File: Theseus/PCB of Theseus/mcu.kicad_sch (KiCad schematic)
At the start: 19 parts, among them J5 Programmer, U6 STM32H750VBTx, U8 MX25L25645G

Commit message: Theseus_Dev_Rev2
It's still the same PCB
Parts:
- removed C10, C11, C12, C13, C14, C15, C22, C9: 100n, Capacitor_SMD:C_0603_1608Metric_Pad1.08x0.95mm_HandSolder, symbol Device:C_Small_US
- removed C16: 4.7u, Capacitor_SMD:C_0603_1608Metric_Pad1.08x0.95mm_HandSolder, symbol Device:C_Small_US
- removed C17: 1u, Capacitor_SMD:C_0402_1005Metric_Pad0.74x0.62mm_HandSolder, symbol Device:C_Small_US
- removed C7, C8: 2.2u, Capacitor_SMD:C_0603_1608Metric_Pad1.08x0.95mm_HandSolder, symbol Device:C_Small_US
- added C10, C11, C12, C13, C14, C15, C22, C9: 100n, Capacitor_SMD:C_0805_2012Metric_Pad1.18x1.45mm_HandSolder, symbol Device:C
- added C16: 4.7u, Capacitor_SMD:C_0805_2012Metric_Pad1.18x1.45mm_HandSolder, symbol Device:C
- added C17: 1n, Capacitor_SMD:C_0805_2012Metric_Pad1.18x1.45mm_HandSolder, symbol Device:C
- added C7, C8: 2.2u, Capacitor_SMD:C_0805_2012Metric_Pad1.18x1.45mm_HandSolder, symbol Device:C
- added FB1: FerriteBead, Resistor_SMD:R_0805_2012Metric_Pad1.20x1.40mm_HandSolder, symbol Device:FerriteBead
- J5: value Programmer -> Programmer GRPB022VWQS-RC
- R44, R45: footprint Resistor_SMD:R_0603_1608Metric_Pad0.98x0.95mm_HandSolder -> Resistor_SMD:R_0805_2012Metric_Pad1.20x1.40mm_HandSolder; symbol Device:R_Small_US -> Device:R_US
- U8: footprint Package_SO:SOIC-16W_7.5x10.3mm_P1.27mm -> Package_SO:SOIC-8_5.3x5.3mm_P1.27mm
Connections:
- net +3.3V: now also U8.8 (VCC), C10.1, C11.1, C12.1, C13.1, C14.1, C15.1, C16.1, C17.1, C9.1, FB1.1; no longer U6.21 (VDDA), U8.2 (VCC)
- net GND: now also U8.4 (GND), C10.2, C11.2, C12.2, C13.2, C14.2, C15.2, C16.2, C17.2, C22.2, C7.2, C8.2, C9.2; no longer U8.10 (GND)
- net LED_BLUE: now also U6.57 (PD10); no longer U6.28 (PA4)
- net LED_RED: now also U6.56 (PD9); no longer U6.29 (PA5)
- net MEM_~{RESET}: now also U8.7 (RESET#/SIO3); no longer U8.3 (RESET#)
- net SPI_MISO: now also U8.2 (SO/SIO1); no longer U8.8 (SO/SIO1)
- net SPI_MOSI: now also U8.5 (SI/SIO0); no longer U8.15 (SI/SIO0)
- net SPI_NSS: now also U8.1 (CS#); no longer U8.7 (CS#)
- net SPI_SCK: now also U8.6 (SCLK); no longer U8.16 (SCLK)
- net at U6.14 (NRST): now also C22.1
- net TC1_SI: now reaches U6.33 (PC5)
- net at U6.48 (VCAP): now also C7.1
- net at U6.73 (VCAP): now also C8.1
- net RTD_1 renamed TC3
- net RTD_2 renamed TC2-
- net RTD_3 renamed TC2+
- new net: FB1.2, U6.21 (VDDA)
- new net TC1_NSS: U6.28 (PA4)
- new net TC1_SCK: U6.29 (PA5)
- no-connect marks 63 -> 52
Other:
- note added: "TC1 using SPI1"
- note added: "Using SPI2 for flash memory"
- note removed: "Using SPI2"

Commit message: Minor routing changes
Still the same PCB
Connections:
- net TC1_SI: now also U6.30 (PA6); no longer U6.33 (PC5)
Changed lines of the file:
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@@
-	)
-	(no_connect
-		(at 115.57 53.34)
 	)
 	(no_connect
 		(at 115.57 66.04)
+	)
+	(no_connect
+		(at 115.57 137.16)
 	)
 	(no_connect
@@
 	(hierarchical_label "TC1_SI"
 		(shape input)
-		(at 115.57 137.16 0)
-		(effects
-			(font
+		(at 115.57 53.34 0)
+		(effects
+			(font

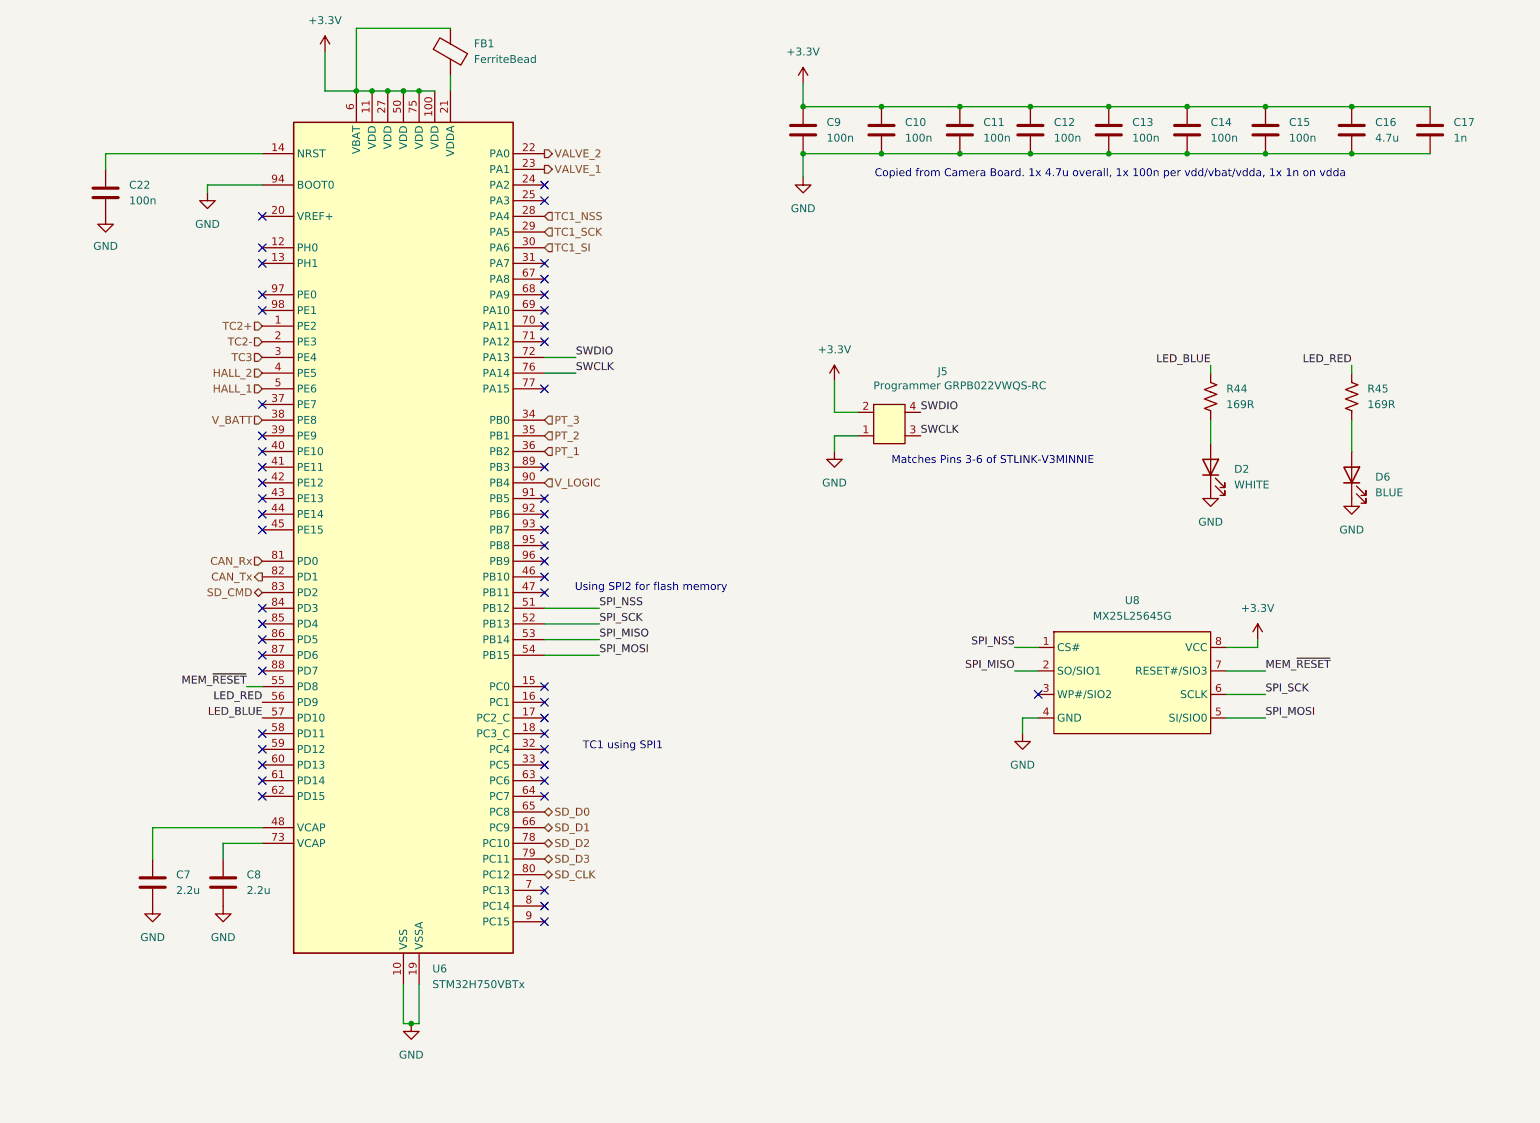
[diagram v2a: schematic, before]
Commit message: Fixes V3
- Copied Ferrite Bead P/N from processor
- Added external oscillator
- Made status LED pins pull-down
- Copied processor programming header
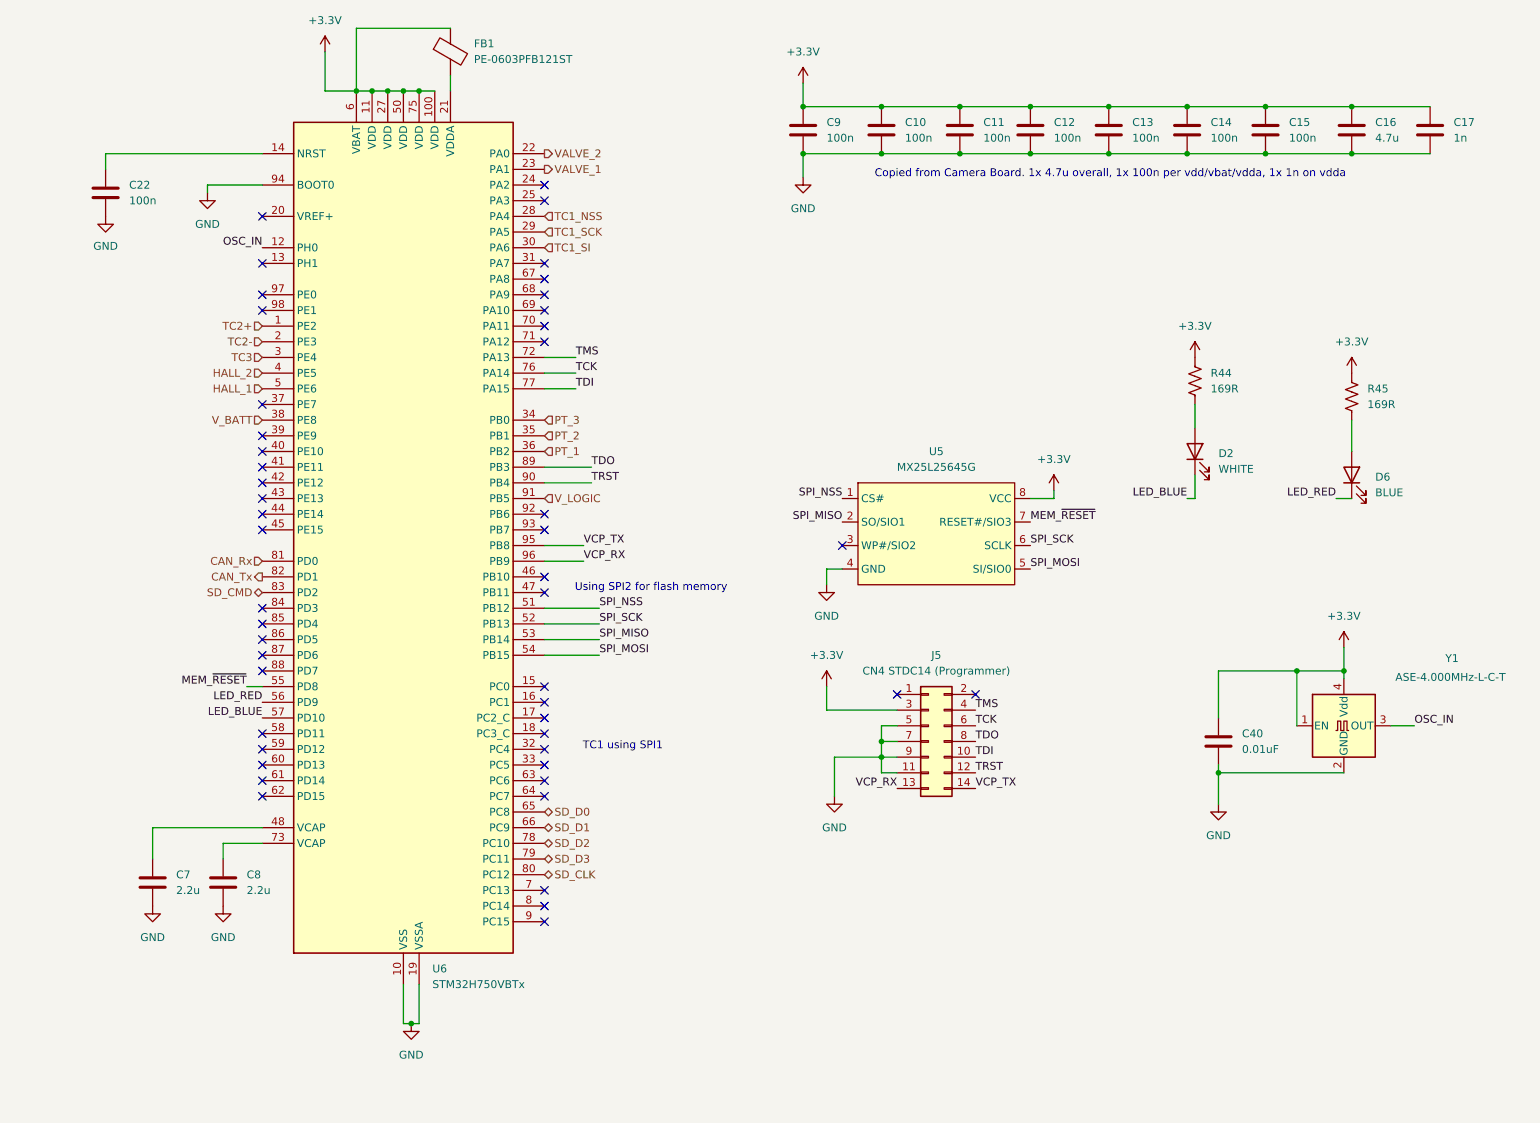
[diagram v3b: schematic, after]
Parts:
- removed J5: Programmer GRPB022VWQS-RC, Connector_PinHeader_1.27mm:PinHeader_2x02_P1.27mm_Vertical_SMD, symbol FYDP_Library:Programmer
- removed U8: MX25L25645G, Package_SO:SOIC-8_5.3x5.3mm_P1.27mm, symbol FYDP_Library:MX25L25645G
- added C40: 0.01uF, Capacitor_SMD:C_0805_2012Metric_Pad1.18x1.45mm_HandSolder, symbol Device:C
- added J5: CN4 STDC14 (Programmer), Connector_PinHeader_1.27mm:PinHeader_2x07_P1.27mm_Vertical_SMD, symbol Connector_Generic:Conn_02x07_Odd_Even
- added U5: MX25L25645G, Package_SO:SOIC-8_5.3x5.3mm_P1.27mm, symbol FYDP_Library:MX25L25645G
- added Y1: ASE-4.000MHz-L-C-T, Oscillator:Oscillator_SMD_Abracon_ASE-4Pin_3.2x2.5mm, symbol Oscillator:ASE-xxxMHz
- D6: footprint Diode_SMD:D_0603_1608Metric_Pad1.05x0.95mm_HandSolder -> Diode_SMD:D_1206_3216Metric_Pad1.42x1.75mm_HandSolder
- FB1: value FerriteBead -> PE-0603PFB121ST; footprint Resistor_SMD:R_0805_2012Metric_Pad1.20x1.40mm_HandSolder -> Resistor_SMD:R_0603_1608Metric_Pad0.98x0.95mm_HandSolder
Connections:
- net +3.3V: now also R44.1, R45.1, C40.1, J5.3 (Pin_3), U5.8 (VCC), Y1.1 (EN), Y1.4 (Vdd)
- net GND: now also C40.2, J5.11 (Pin_11), J5.5 (Pin_5), J5.7 (Pin_7), J5.9 (Pin_9), U5.4 (GND), Y1.2 (GND); no longer D2.1 (K), D6.1 (K)
- net LED_BLUE: now also D2.1 (K); no longer R44.1
- net LED_RED: now also D6.1 (K); no longer R45.1
- net MEM_~{RESET}: now also U5.7 (RESET#/SIO3)
- net SPI_MISO: now also U5.2 (SO/SIO1)
- net SPI_MOSI: now also U5.5 (SI/SIO0)
- net SPI_NSS: now also U5.1 (CS#)
- net SPI_SCK: now also U5.6 (SCLK)
- net V_LOGIC: now also U6.91 (PB5); no longer U6.90 (PB4)
- net OSC_IN: now reaches U6.12 (PH0)
- net OSC_IN: now also Y1.3 (OUT)
- net TDI: now reaches U6.77 (PA15)
- net TDI: now also J5.10 (Pin_10)
- net TDO: now reaches U6.89 (PB3)
- net TDO: now also J5.8 (Pin_8)
- net VCP_TX: now reaches U6.95 (PB8)
- net VCP_TX: now also J5.14 (Pin_14)
- net VCP_RX: now reaches U6.96 (PB9)
- net VCP_RX: now also J5.13 (Pin_13)
- net SWCLK renamed TCK
- net TCK: now also J5.6 (Pin_6)
- net SWDIO renamed TMS
- net TMS: now also J5.4 (Pin_4)
- new net TRST: J5.12 (Pin_12), U6.90 (PB4)
- no-connect marks 52 -> 48
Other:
- note removed: "Matches Pins 3-6 of STLINK-V3MINNIE"
- moved on the sheet: D2, R44

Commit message: Flight design, first pass
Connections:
- net PT_1: now also U6.35 (PB1); no longer U6.36 (PB2)
- net PT_2: now also U6.36 (PB2); no longer U6.35 (PB1)
- net TC2+: no longer names the net of U6.1 (PE2)
- net TC2-: no longer names the net of U6.2 (PE3)
- net TC3: no longer names the net of U6.3 (PE4)
- no-connect marks 48 -> 51
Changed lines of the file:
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@@
 	(text "TC1 using SPI1"
 		(exclude_from_sim no)
-		(at 128.27 134.112 0)
+		(at 125.476 56.388 0)
 		(effects
 			(font
@@
 	)
 	(no_connect
+		(at 69.85 68.58)
+	)
+	(no_connect
+		(at 69.85 66.04)
+	)
+	(no_connect
 		(at 69.85 96.52)
 	)
@@
 	(no_connect
 		(at 69.85 48.26)
+	)
+	(no_connect
+		(at 69.85 71.12)
 	)
 	(no_connect
@@
 		)
 	)
-	(hierarchical_label "TC3"
-		(shape input)
-		(at 69.85 71.12 180)
-		(effects
-			(font
-				(size 1.27 1.27)
-			)
-			(justify right)
-		)
-	)
 	(hierarchical_label "TC1_NSS"
 		(shape input)
@@
 		)
 	)
-	(hierarchical_label "TC2+"
-		(shape input)
-		(at 69.85 66.04 180)
-		(effects
-			(font
-				(size 1.27 1.27)
-			)
-			(justify right)
-		)
-	)
 	(hierarchical_label "PT_1"
 		(shape input)
-		(at 115.57 86.36 0)
+		(at 115.57 83.82 0)
 		(effects
 			(font
@@
 	(hierarchical_label "PT_2"
 		(shape input)
-		(at 115.57 83.82 0)
+		(at 115.57 86.36 0)
 		(effects
 			(font
@@
 		)
 	)
-	(hierarchical_label "TC2-"
-		(shape input)
-		(at 69.85 68.58 180)
-		(effects
-			(font
-				(size 1.27 1.27)
-			)
-			(justify right)
-		)
-	)

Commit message: Flight design v1
First pass at flight design
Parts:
- C10, C11, C12, C13, C14, C15, C16, C17, C22, C40, C7, C8, C9: footprint Capacitor_SMD:C_0805_2012Metric_Pad1.18x1.45mm_HandSolder -> Capacitor_SMD:C_0603_1608Metric_Pad1.08x0.95mm_HandSolder
- D2, D6: footprint Diode_SMD:D_1206_3216Metric_Pad1.42x1.75mm_HandSolder -> Diode_SMD:D_0603_1608Metric_Pad1.05x0.95mm_HandSolder
- J5: footprint Connector_PinHeader_1.27mm:PinHeader_2x07_P1.27mm_Vertical_SMD -> Connector_PinSocket_1.27mm:PinSocket_2x07_P1.27mm_Vertical_SMD
- R44, R45: footprint Resistor_SMD:R_0805_2012Metric_Pad1.20x1.40mm_HandSolder -> Resistor_SMD:R_0603_1608Metric_Pad0.98x0.95mm_HandSolder
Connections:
- net PT_1: now also U6.36 (PB2); no longer U6.35 (PB1)
- net PT_2: now also U6.35 (PB1); no longer U6.36 (PB2)
- net PT6: now reaches U6.40 (PE10)
- net PT5: now reaches U6.41 (PE11)
- net PT4: now reaches U6.42 (PE12)
- no-connect marks 51 -> 48
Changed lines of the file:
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@@
 	(text "TC1 using SPI1"
 		(exclude_from_sim no)
-		(at 125.476 56.388 0)
+		(at 134.112 51.308 0)
 		(effects
 			(font
@@
 	)
 	(no_connect
-		(at 69.85 86.36)
+		(at 69.85 116.84)
 	)
 	(no_connect
@@
 	)
 	(no_connect
-		(at 69.85 121.92)
-	)
-	(no_connect
-		(at 69.85 116.84)
+		(at 172.72 125.73)
 	)
 	(no_connect
-		(at 172.72 125.73)
+		(at 69.85 119.38)
 	)
 	(no_connect
@@
 	)
 	(no_connect
-		(at 69.85 88.9)
-	)
-	(no_connect
 		(at 115.57 129.54)
 	)
@@
 	)
 	(no_connect
-		(at 69.85 91.44)
-	)
-	(no_connect
 		(at 69.85 134.62)
 	)
@@
 	)
 	(no_connect
-		(at 69.85 119.38)
-	)
-	(no_connect
 		(at 69.85 55.88)
 	)
@@
 	)
 	(no_connect
+		(at 69.85 121.92)
+	)
+	(no_connect
 		(at 115.57 137.16)
 	)
@@
 		)
 	)
+	(hierarchical_label "PT6"
+		(shape input)
+		(at 69.85 86.36 180)
+		(effects
+			(font
+				(size 1.27 1.27)
+			)
+			(justify right)
+		)
+	)
 	(hierarchical_label "V_BATT"
 		(shape input)
@@
 	(hierarchical_label "PT_1"
 		(shape input)
-		(at 115.57 83.82 0)
+		(at 115.57 86.36 0)
 		(effects
 			(font
@@
 	(hierarchical_label "PT_2"
 		(shape input)
-		(at 115.57 86.36 0)
+		(at 115.57 83.82 0)
 		(effects
 			(font
@@
 		)
 	)
+	(hierarchical_label "PT4"
+		(shape input)
+		(at 69.85 91.44 180)
+		(effects
+			(font
+				(size 1.27 1.27)
+			)
+			(justify right)
+		)
+	)
 	(hierarchical_label "TC1_SI"
 		(shape input)
@@
 		)
 	)
+	(hierarchical_label "PT5"
+		(shape input)
+		(at 69.85 88.9 180)
+		(effects
+			(font
+				(size 1.27 1.27)
+			)
+			(justify right)
+		)
+	)
 	(symbol
 		(lib_id "Device:C")
@@
 			)
 		)
-		(property "Footprint" "Capacitor_SMD:C_0805_2012Metric_Pad1.18x1.45mm_HandSolder"
+		(property "Footprint" "Capacitor_SMD:C_0603_1608Metric_Pad1.08x0.95mm_HandSolder"
 			(at 53.0352 160.02 0)
 			(effects
@@
 			)
 		)
-		(property "Footprint" "Capacitor_SMD:C_0805_2012Metric_Pad1.18x1.45mm_HandSolder"
+		(property "Footprint" "Capacitor_SMD:C_0603_1608Metric_Pad1.08x0.95mm_HandSolder"
 			(at 195.2752 38.1 0)
 			(effects
@@
 			)
 		)
-		(property "Footprint" "Capacitor_SMD:C_0805_2012Metric_Pad1.18x1.45mm_HandSolder"
+		(property "Footprint" "Capacitor_SMD:C_0603_1608Metric_Pad1.08x0.95mm_HandSolder"
 			(at 183.8452 38.1 0)
 			(effects
@@
 			)
 		)
-		(property "Footprint" "Resistor_SMD:R_0805_2012Metric_Pad1.20x1.40mm_HandSolder"
+		(property "Footprint" "Resistor_SMD:R_0603_1608Metric_Pad0.98x0.95mm_HandSolder"
 			(at 247.396 77.724 90)
 			(effects
@@
 			)
 		)
-		(property "Footprint" "Connector_PinHeader_1.27mm:PinHeader_2x07_P1.27mm_Vertical_SMD"
+		(property "Footprint" "Connector_PinSocket_1.27mm:PinSocket_2x07_P1.27mm_Vertical_SMD"
 			(at 177.8 133.35 0)
 			(effects
@@
 			)
 		)
-		(property "Footprint" "Diode_SMD:D_1206_3216Metric_Pad1.42x1.75mm_HandSolder"
+		(property "Footprint" "Diode_SMD:D_0603_1608Metric_Pad1.05x0.95mm_HandSolder"
 			(at 220.98 86.36 0)
 			(effects
@@
 			)
 		)
-		(property "Footprint" "Capacitor_SMD:C_0805_2012Metric_Pad1.18x1.45mm_HandSolder"
+		(property "Footprint" "Capacitor_SMD:C_0603_1608Metric_Pad1.08x0.95mm_HandSolder"
 			(at 233.3752 38.1 0)
 			(effects
@@
 			)
 		)
-		(property "Footprint" "Capacitor_SMD:C_0805_2012Metric_Pad1.18x1.45mm_HandSolder"
+		(property "Footprint" "Capacitor_SMD:C_0603_1608Metric_Pad1.08x0.95mm_HandSolder"
 			(at 45.4152 48.26 0)
 			(effects
@@
 			)
 		)
-		(property "Footprint" "Capacitor_SMD:C_0805_2012Metric_Pad1.18x1.45mm_HandSolder"
+		(property "Footprint" "Capacitor_SMD:C_0603_1608Metric_Pad1.08x0.95mm_HandSolder"
 			(at 171.1452 38.1 0)
 			(effects
@@
 			)
 		)
-		(property "Footprint" "Resistor_SMD:R_0805_2012Metric_Pad1.20x1.40mm_HandSolder"
+		(property "Footprint" "Resistor_SMD:R_0603_1608Metric_Pad0.98x0.95mm_HandSolder"
 			(at 221.996 75.184 90)
 			(effects
@@
 			)
 		)
-		(property "Footprint" "Capacitor_SMD:C_0805_2012Metric_Pad1.18x1.45mm_HandSolder"
+		(property "Footprint" "Capacitor_SMD:C_0603_1608Metric_Pad1.08x0.95mm_HandSolder"
 			(at 260.0452 38.1 0)
 			(effects
@@
 			)
 		)
-		(property "Footprint" "Capacitor_SMD:C_0805_2012Metric_Pad1.18x1.45mm_HandSolder"
+		(property "Footprint" "Capacitor_SMD:C_0603_1608Metric_Pad1.08x0.95mm_HandSolder"
 			(at 64.4652 160.02 0)
 			(effects
@@
 			)
 		)
-		(property "Footprint" "Capacitor_SMD:C_0805_2012Metric_Pad1.18x1.45mm_HandSolder"
+		(property "Footprint" "Capacitor_SMD:C_0603_1608Metric_Pad1.08x0.95mm_HandSolder"
 			(at 207.9752 38.1 0)
 			(effects
@@
 			)
 		)
-		(property "Footprint" "Capacitor_SMD:C_0805_2012Metric_Pad1.18x1.45mm_HandSolder"
+		(property "Footprint" "Capacitor_SMD:C_0603_1608Metric_Pad1.08x0.95mm_HandSolder"
 			(at 225.7552 137.16 0)
 			(effects
@@
 			)
 		)
-		(property "Footprint" "Capacitor_SMD:C_0805_2012Metric_Pad1.18x1.45mm_HandSolder"
+		(property "Footprint" "Capacitor_SMD:C_0603_1608Metric_Pad1.08x0.95mm_HandSolder"
 			(at 158.4452 38.1 0)
 			(effects
@@
 			)
 		)
-		(property "Footprint" "Capacitor_SMD:C_0805_2012Metric_Pad1.18x1.45mm_HandSolder"
+		(property "Footprint" "Capacitor_SMD:C_0603_1608Metric_Pad1.08x0.95mm_HandSolder"
 			(at 247.3452 38.1 0)
 			(effects
@@
 			)
 		)
-		(property "Footprint" "Capacitor_SMD:C_0805_2012Metric_Pad1.18x1.45mm_HandSolder"
+		(property "Footprint" "Capacitor_SMD:C_0603_1608Metric_Pad1.08x0.95mm_HandSolder"
 			(at 220.6752 38.1 0)
 			(effects
@@
 			)
 		)
-		(property "Footprint" "Diode_SMD:D_1206_3216Metric_Pad1.42x1.75mm_HandSolder"
+		(property "Footprint" "Diode_SMD:D_0603_1608Metric_Pad1.05x0.95mm_HandSolder"
 			(at 246.38 90.17 0)
 			(effects
